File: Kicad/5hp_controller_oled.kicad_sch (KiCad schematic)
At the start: 14 parts, among them IC1 TCA9548, J1 SSD1306, J10 ToSateliteModule, J16 ToMAINModule, J2 AS5600_2_PWR, J3 Conn_01x02_Socket, J4 AS5600_2_PWR, J5 AS5600_2_PWR, J6 Conn_01x01_Socket, J7 Conn_01x02_Socket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

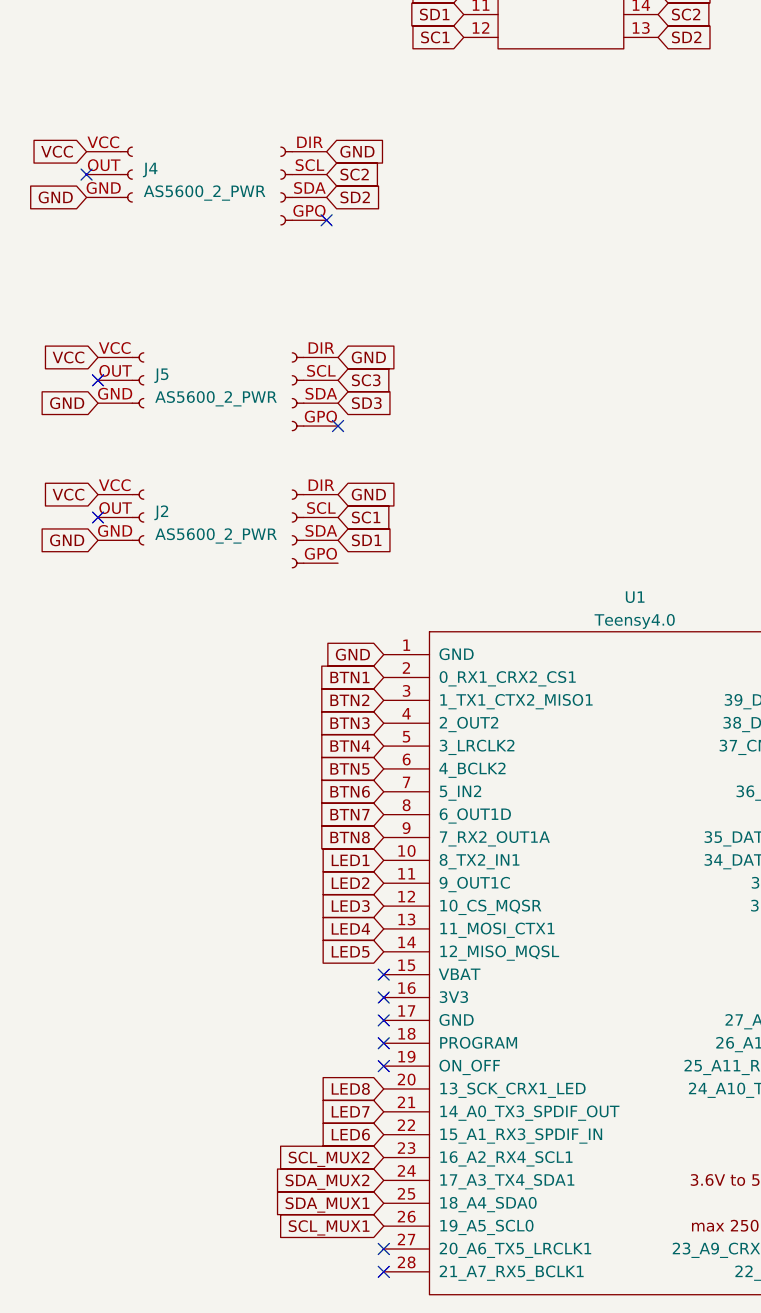
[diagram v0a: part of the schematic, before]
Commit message: Fixed pcb errors (wrong footprint TCA, freed up pin 13)
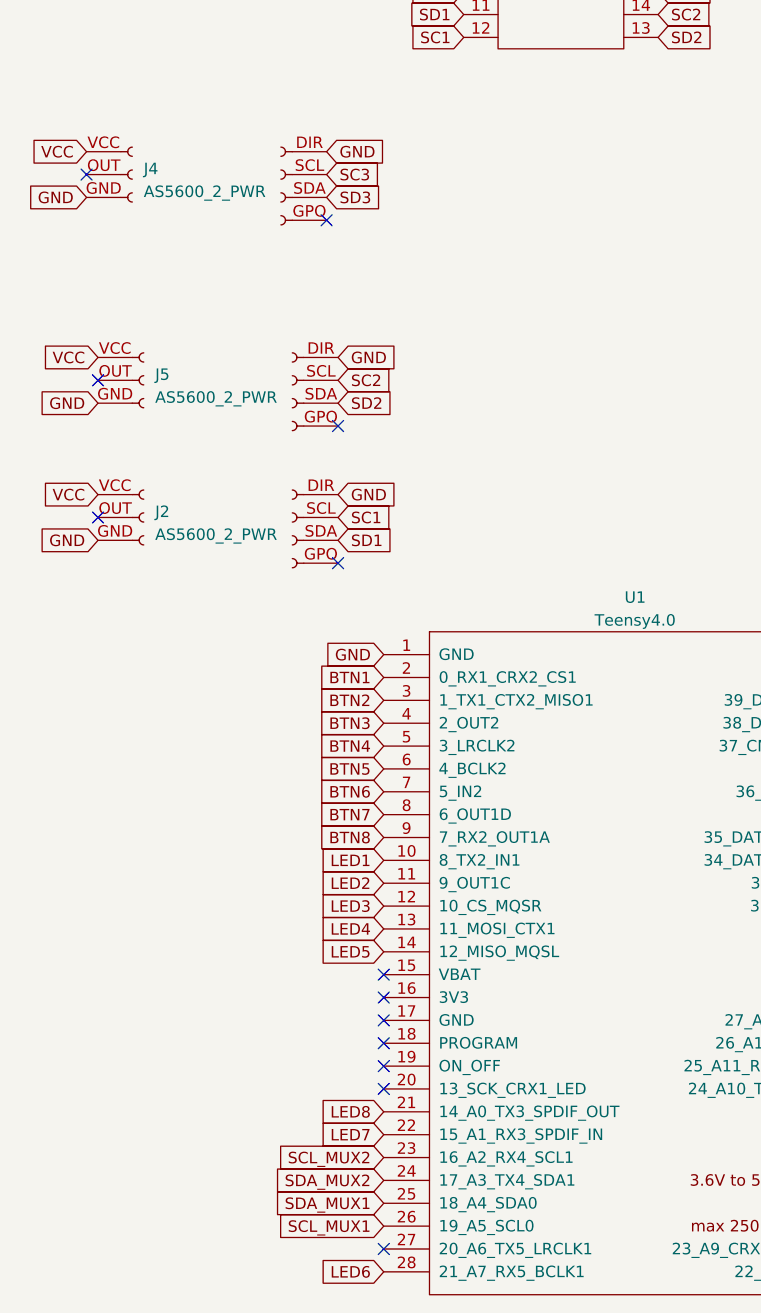
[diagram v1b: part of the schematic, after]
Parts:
- IC1: footprint SSD1306:DIP-28_W17.48mm_Socket -> SSD1306:DIP-24_W9.xx mm_Socket
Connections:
- net LED6: now also U1.28 (21_A7_RX5_BCLK1); no longer U1.22 (15_A1_RX3_SPDIF_IN)
- net LED7: now also U1.22 (15_A1_RX3_SPDIF_IN); no longer U1.21 (14_A0_TX3_SPDIF_OUT)
- net LED8: now also U1.21 (14_A0_TX3_SPDIF_OUT); no longer U1.20 (13_SCK_CRX1_LED)
- net SC2: now also J5.SCL (Pin_5); no longer J4.SCL (Pin_5)
- net SC3: now also J4.SCL (Pin_5); no longer J5.SCL (Pin_5)
- net SD2: now also J5.SDA (Pin_6); no longer J4.SDA (Pin_6)
- net SD3: now also J4.SDA (Pin_6); no longer J5.SDA (Pin_6)
- no-connect marks 43 -> 44
